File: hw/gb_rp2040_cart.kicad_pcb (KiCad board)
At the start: 4 copper layers, 51.4 x 60.5 mm, 75 parts, among them J1 GameBoy_Cartridge, J2 USB_C_Receptacle_USB2.0, Q1 SI2301CDS-T1-GE3, Q2 N-Channel, SW1 SW_DPST, SW2 SW_Push, U1 SN74LVC8T245PW, U10 MB85RC256VPNF-G-JNERE1, U11 DS3231M, U2 SN74LVC8T245PW, U3 TXU0104, U4 SN74LVC8T245PW, U5 W25Q128JVSIQ, U6 RP2040, U7 XC6206P332MR, U9 PCA9536D, Y1 Crystal_GND24

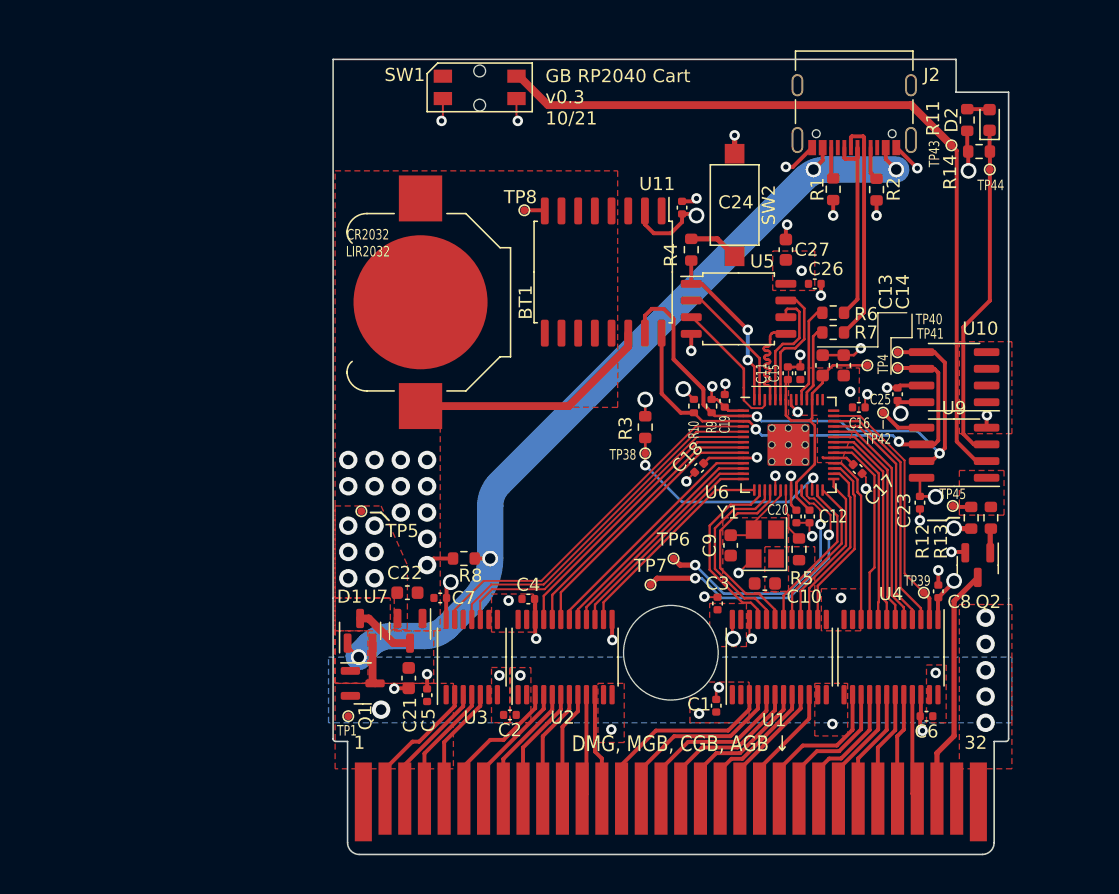
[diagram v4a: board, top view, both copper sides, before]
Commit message: hw: use CR2032 footprint & larger testpoints
Signed-off-by: Mahyar Koshkouei <mk@deltabeard.com>
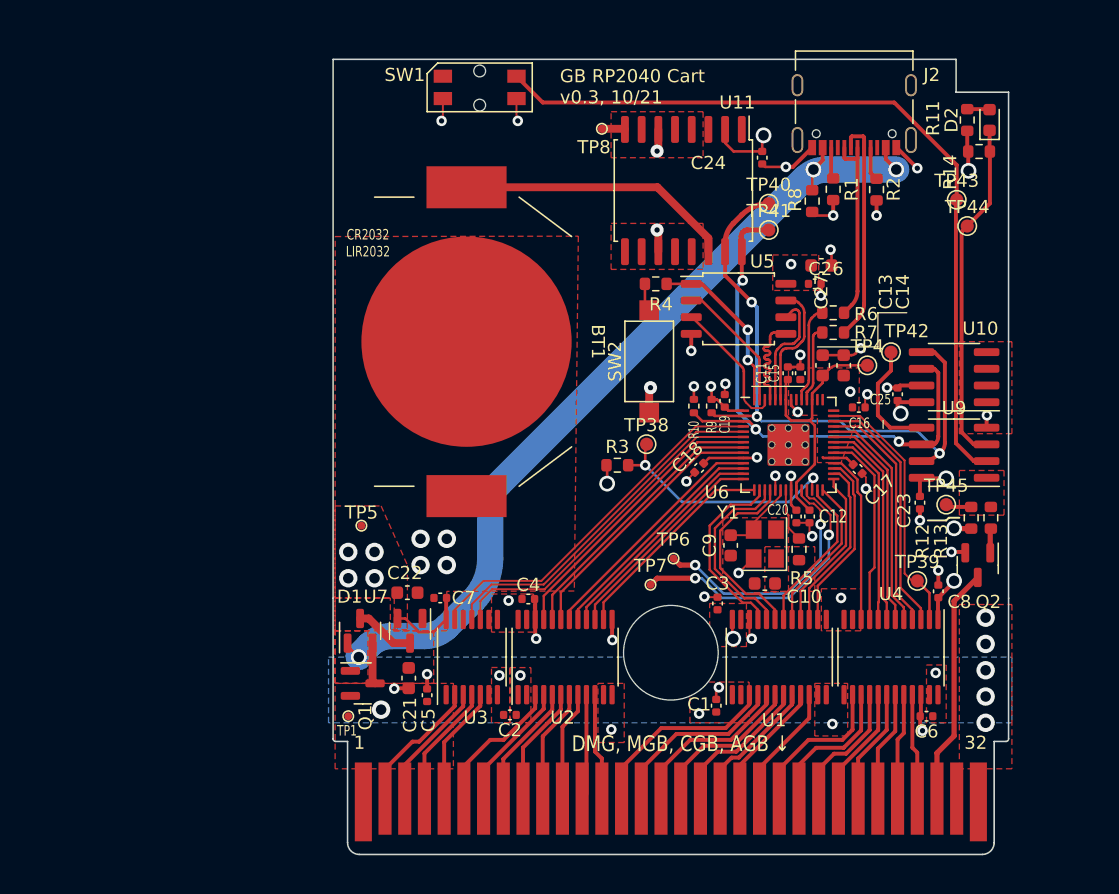
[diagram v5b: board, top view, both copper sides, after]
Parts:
- BT1: footprint Battery:BatteryHolder_Keystone_3000_1x12mm -> Project_Specific:MY-2032-11
- TP38, TP39, TP40, TP41, TP42, TP43, TP44, TP45: footprint Project_Specific:TestPoint_Pad_D0.5mm -> TestPoint:TestPoint_Pad_D1.0mm
- moved R8 38.0 mm to (94.8, 48.3), turned to -90 degrees
- moved TP40 15.0 mm to (91.5, 48.5)
- moved TP41 14.4 mm to (91.5, 50.5)
- moved SW2 13.6 mm to (82.4, 60.5), turned to 90 degrees
- moved U11 8.70 mm to (85.0, 47.5)
- moved TP8 8.56 mm to (78.8, 42.8)
- moved C24 7.19 mm to (91.0, 45.0), turned to -90 degrees
- moved TP42 4.64 mm to (100.8, 59.8)
- moved TP44 4.63 mm to (106.6, 50.2)
- moved BT1 4.61 mm to (68.5, 59.0)
- moved TP43 4.16 mm to (105.8, 48.2)
- moved R4 3.75 mm to (82.9, 54.6), turned to 0 degrees
- moved R3 3.60 mm to (80.0, 68.4), turned to 180 degrees
- moved C27 2.95 mm to (95.5, 53.2), turned to 0 degrees
- moved TP5 1.10 mm to (60.5, 73.0)
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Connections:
- SW1 pad 1: /Peripherals/SWITCH -> (no net)
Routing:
- net /Peripherals/STAT_LED: track 47.3 -> 26.1 mm
- net /Peripherals/SWITCH: track 75.8 -> 60.4 mm
- net I^{2}C_{SCL}: track 35.8 -> 44.0 mm, vias 2 -> 3
- net I^{2}C_{SDA}: track 53.8 -> 47.7 mm, vias 2 -> 3
- net Net-(TP42-Pad1): track 3.40 -> 8.93 mm
- net GND: track 54.0 -> 58.0 mm, vias 54 -> 47
- net Net-(R7-Pad1): track 9.56 -> 5.85 mm
- net +3V3: track 42.3 -> 45.2 mm, vias 23 -> 20
- net /A8: track 15.2 -> 12.5 mm
- net /A14: track 9.82 -> 7.28 mm
- net /A10: track 13.3 -> 10.8 mm
- net /A11: track 12.5 -> 9.95 mm
- net /A12: track 11.6 -> 9.10 mm
- net /A9: track 14.1 -> 11.7 mm
- net /A13: track 10.7 -> 8.25 mm
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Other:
- board text added: "GB RP2040 Cart v0.3, 10/21"
- board text removed: "GB RP2040 Cart v0.3 10/21"
- board text removed: "Order #"

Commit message: More attempts
Signed-off-by: Mahyar Koshkouei <mk@deltabeard.com>
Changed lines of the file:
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@@
   (gr_line (start 100.2 65.6) (end 100.2 65) (layer "F.SilkS") (width 0.1))
   (gr_line (start 105.2 72.4) (end 106 72.4) (layer "F.SilkS") (width 0.15))
+  (gr_line (start 103.6 40.4) (end 109 40.4) (layer "F.SilkS") (width 0.1))
   (gr_line (start 90.2 62.4) (end 94.2 62.4) (layer "F.SilkS") (width 0.1))
   (gr_line (start 99.8 59.4) (end 95.2 59.4) (layer "F.SilkS") (width 0.1))
@@
   (gr_line (start 115 41) (end 53 41) (layer "Eco1.User") (width 0.1))
   (gr_line (start 115 34) (end 53 34) (layer "Eco1.User") (width 0.1))
-  (gr_line (start 103.6 40.4) (end 109 40.4) (layer "Eco2.User") (width 0.1))
   (gr_text "Flash cart compatible with DMG, MGB, CGB, AGB. Unlicensed product.\nUses RP2040 with 16MiB NOR, 32KiB FRAM, RTC, USB-C.\nDesign: United Kingdom, Assembly: P.R. China\nCopyright © 2021 Mahyar Koshkouei; Not for resale." (at 107 94) (layer "B.SilkS")
     (effects (font (size 1 0.85) (thickness 0.14)) (justify left mirror))
@@
   (segment (start 93.925 85.8625) (end 93.925 86.599999) (width 0.3) (layer "F.Cu") (net 27))
   (segment (start 93.925 86.599999) (end 89.297851 91.227148) (width 0.3) (layer "F.Cu") (net 27))
-  (segment (start 94.575 85.8625) (end 94.575 87.642168) (width 0.3) (layer "F.Cu") (net 28))
-  (segment (start 94.575 87.642168) (end 90.797851 91.419317) (width 0.3) (layer "F.Cu") (net 28))
+  (segment (start 94.575 85.8625) (end 94.575 86.895362) (width 0.3) (layer "F.Cu") (net 28))
+  (segment (start 94.575 86.895362) (end 90.797851 90.672511) (width 0.3) (layer "F.Cu") (net 28))
+  (segment (start 90.797851 90.672511) (end 90.797851 91.419317) (width 0.3) (layer "F.Cu") (net 28))
   (segment (start 97.875 88.525) (end 97.1 89.3) (width 0.3) (layer "F.Cu") (net 29))
   (segment (start 97.875 85.8625) (end 97.875 88.525) (width 0.3) (layer "F.Cu") (net 29))

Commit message: hw: begin layout
Signed-off-by: Mahyar Koshkouei <mk@deltabeard.com>
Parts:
- removed C27: 1u, Capacitor_SMD:C_0603_1608Metric
- removed R6: 27.4R, Resistor_SMD:R_0603_1608Metric
- removed SW1: SW_DPST, Project_Specific:K2-1114SA-A4SW-06
- removed TP38, TP39, TP40, TP41, TP42, TP43, TP44, TP45: TestPoint_Small, TestPoint:TestPoint_Pad_D1.0mm
- removed TP4, TP5: TestPoint, TestPoint:TestPoint_Pad_D1.0mm
- removed TP7: SWDIO, TestPoint:TestPoint_Pad_D1.0mm
- removed U10: MB85RC256VPNF-G-JNERE1, Package_SO:SOIC-8_3.9x4.9mm_P1.27mm
- removed U11: DS3231M, Package_SO:SOIC-16W_7.5x10.3mm_P1.27mm
- added SW3: SW_SPST, Project_Specific:TS-1037-A10B3-D2, F.Cu at (61.9, 39.5)
- added TP10: SWCLK, TestPoint:TestPoint_Pad_D1.0mm, F.Cu at (101.8, 45.2)
- added TP11: SWDIO, TestPoint:TestPoint_Pad_D1.0mm, F.Cu at (101.8, 58.1)
- added TP12: GND, TestPoint:TestPoint_Pad_D1.0mm, F.Cu at (101.8, 51.6)
- added TP13: TestPoint_Small, TestPoint:TestPoint_Pad_D1.0mm, F.Cu at (101.8, 53.8)
- added TP14: TestPoint_Small, TestPoint:TestPoint_Pad_D1.0mm, F.Cu at (101.8, 56.0)
- added TP15: TestPoint_Small, TestPoint:TestPoint_Pad_D1.0mm, F.Cu at (101.8, 60.3)
- added TP16: TestPoint_Small, TestPoint:TestPoint_Pad_D1.0mm, F.Cu at (101.8, 64.6)
- added TP9: TestPoint, TestPoint:TestPoint_Pad_D1.0mm, F.Cu at (101.8, 62.4)
- added U8: DS1307Z+, Package_SO:SO-8_3.9x4.9mm_P1.27mm, F.Cu at (60.5, 49.8)
- added Y2: 32.768k-12.5pF, Project_Specific:Crystal_DS26_D2.0mm_L6.0mm_Horizontal_1EP_style1, F.Cu at (65.3, 49.5)
- C10: value 30p -> 100n; footprint Capacitor_SMD:C_0603_1608Metric -> Capacitor_SMD:C_0402_1005Metric
- C11, C12: value 100n -> 30p; footprint Capacitor_SMD:C_0402_1005Metric -> Capacitor_SMD:C_0603_1608Metric
- C13, C14, C21: value 1u -> 100n; footprint Capacitor_SMD:C_0603_1608Metric -> Capacitor_SMD:C_0402_1005Metric
- C15, C23, C24: value 100n -> 1u; footprint Capacitor_SMD:C_0402_1005Metric -> Capacitor_SMD:C_0603_1608Metric
- C9: value 30p -> 1u
- R1, R2: value 5k1 -> 25k; footprint Resistor_SMD:R_0603_1608Metric -> Resistor_SMD:R_0402_1005Metric
- R10, R9: value 4k7 -> 27.4R; footprint Resistor_SMD:R_0402_1005Metric -> Resistor_SMD:R_0603_1608Metric
- R11: value 330R -> 100k
- R14: value 100k -> 330R
- R3: value 100k -> 25k; footprint Resistor_SMD:R_0603_1608Metric -> Resistor_SMD:R_0402_1005Metric
- R4, R5: value 1k -> 5k1
- R7: value 27.4R -> 1k
- R8: value 100k -> 1k
- SW2: value SW_Push -> SW_DIP_x04; footprint Button_Switch_SMD:SW_SPST_CK_RS282G05A3 -> Button_Switch_SMD:SW_DIP_SPSTx04_Slide_6.7x11.72mm_W8.61mm_P2.54mm_LowProfile
- TP1: value TestPoint -> TestPoint_Small
- TP6: value SWCLK -> TestPoint
- TP8: value GND -> TestPoint
- U9: value PCA9536D -> MB85RS256B
- moved R11 79.1 mm to (38.2, 82.0)
- moved C23 65.2 mm to (38.2, 79.0)
- moved C6 62.1 mm to (41.5, 85.0)
- moved C8 61.1 mm to (43.3, 76.5)
- moved C24 57.1 mm to (40.8, 72.3), turned to 180 degrees
- moved R1 51.3 mm to (57.2, 80.5)
- moved R2 45.8 mm to (65.4, 77.8), turned to 90 degrees
- moved U9 42.1 mm to (64.2, 59.8), turned to 0 degrees
- moved R8 41.4 mm to (58.4, 68.0), turned to 0 degrees
- moved C11 41.4 mm to (52.6, 70.5), turned to -90 degrees
- moved C25 38.6 mm to (64.2, 52.2), turned to 0 degrees
- moved C13 38.0 mm to (58.8, 70.2), turned to 180 degrees
- moved C12 37.0 mm to (57.6, 72.3), turned to 90 degrees
- moved TP6 36.9 mm to (101.8, 43.0)
- moved Y1 36.3 mm to (55.1, 70.5)
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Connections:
- BT1 pad 1: Net-(BT1-Pad1) -> V_{BAT}
- C1 pad 1: GB_5V -> +3V3
- C10 pad 1: GND -> +3V3
- C10 pad 2: Net-(C10-Pad2) -> GND
- C11 pad 1: +1V1 -> Net-(C11-Pad1)
- C12 pad 1: +1V1 -> GND
- C12 pad 2: GND -> Net-(C12-Pad2)
- C14 pad 1: +3V3 -> +1V1
- C2 pad 1: GB_5V -> +3V3
- C21 pad 1: +5V -> +3V3
- C22 pad 1: +3V3 -> +1V1
- C23 pad 1: +3V3 -> +5V
- C3 pad 2: +3V3 -> GB_5V
- C4 pad 2: +3V3 -> GB_5V
- C5 pad 1: GB_5V -> GND
- C5 pad 2: GND -> +3V3
- C7 pad 1: GND -> GB_5V
- C7 pad 2: +3V3 -> GND
- C9 pad 1: Net-(C9-Pad1) -> +3V3
- D2 pad 1: /Peripherals/STAT_LED -> Net-(D2-Pad1)
- D2 pad 2: Net-(D2-Pad2) -> STAT_LED
- R1 pad 1: GND -> ADDR1_OE
- R1 pad 2: Net-(J2-PadB5) -> +3V3
- R10 pad 1: I^{2}C_{SCL} -> Net-(R10-Pad1)
- R10 pad 2: +3V3 -> USB_DN
- R11 pad 1: +3V3 -> VBUS
- R11 pad 2: Net-(D2-Pad2) -> GND
- R12 pad 1: /Peripherals/GB_RESET -> GB_RESET
- R13 pad 1: /Peripherals/GB_RESET -> GB_RESET
- R14 pad 1: /Peripherals/STAT_LED -> Net-(D2-Pad1)
- R14 pad 2: +3V3 -> GND
- R2 pad 1: Net-(J2-PadA5) -> ADDR2_OE
- R2 pad 2: GND -> +3V3
- R3 pad 1: /RP2040/RUN -> DATA_OE
- R4 pad 1: /RP2040/USB_BOOT -> GND
- R4 pad 2: /RP2040/QSPI_SS -> Net-(J2-PadB5)
- R5 pad 1: Net-(C10-Pad2) -> Net-(J2-PadA5)
- R5 pad 2: Net-(R5-Pad2) -> GND
- R7 pad 1: Net-(R7-Pad1) -> /RP2040/USB_BOOT
- R7 pad 2: USB_DN -> /RP2040/QSPI_SS
- R8 pad 1: VBUS -> Net-(C12-Pad2)
- R8 pad 2: GND -> Net-(R8-Pad2)
- R9 pad 1: I^{2}C_{SDA} -> Net-(R9-Pad1)
- R9 pad 2: +3V3 -> USB_DP
- SW2 pad 1: GND -> Net-(SW2-Pad1)
- SW2 pad 2: /RP2040/USB_BOOT -> Net-(SW2-Pad2)
- TP1 pad 1: GB_5V -> /A15
- TP6 pad 1: /RP2040/SWCLK -> GB_5V
- TP8 pad 1: GND -> +1V1
- U1 pad 1: GB_5V -> +3V3
- U1 pad 10: /A15 -> 3V3_M0
- U1 pad 14: 3V3_A15 -> /A8
- U1 pad 15: 3V3_A14 -> /A9
- U1 pad 16: 3V3_A13 -> /A10
- U1 pad 17: 3V3_A12 -> /A11
- U1 pad 18: 3V3_A11 -> /A12
- U1 pad 19: 3V3_A10 -> /A13
- U1 pad 2: GB_5V -> GND
- U1 pad 20: 3V3_A9 -> /A14
- U1 pad 21: 3V3_A8 -> /A15
- U1 pad 22: GND -> ADDR2_OE
- U1 pad 23: +3V3 -> GB_5V
- U1 pad 24: +3V3 -> GB_5V
- U1 pad 3: /A8 -> 3V3_M7
- U1 pad 4: /A9 -> 3V3_M6
- U1 pad 5: /A10 -> 3V3_M5
- U1 pad 6: /A11 -> 3V3_M4
- U1 pad 7: /A12 -> 3V3_M3
- U1 pad 8: /A13 -> 3V3_M2
- U1 pad 9: /A14 -> 3V3_M1
- U2 pad 1: GB_5V -> +3V3
- U2 pad 10: /A7 -> 3V3_M0
- U2 pad 14: 3V3_A7 -> /A0
- U2 pad 15: 3V3_A6 -> /A1
- U2 pad 16: 3V3_A5 -> /A2
- U2 pad 17: 3V3_A4 -> /A3
- U2 pad 18: 3V3_A3 -> /A4
- U2 pad 19: 3V3_A2 -> /A5
- U2 pad 2: GB_5V -> GND
- U2 pad 20: 3V3_A1 -> /A6
- U2 pad 21: 3V3_A0 -> /A7
- U2 pad 22: GND -> ADDR1_OE
- U2 pad 23: +3V3 -> GB_5V
- U2 pad 24: +3V3 -> GB_5V
- U2 pad 3: /A0 -> 3V3_M7
- U2 pad 4: /A1 -> 3V3_M6
- U2 pad 5: /A2 -> 3V3_M5
- U2 pad 6: /A3 -> 3V3_M4
- U2 pad 7: /A4 -> 3V3_M3
- U2 pad 8: /A5 -> 3V3_M2
- U2 pad 9: /A6 -> 3V3_M1
- U4 pad 10: 3V3_D0 -> 3V3_M0
- U4 pad 22: GND -> DATA_OE
- U4 pad 3: 3V3_D7 -> 3V3_M7
- U4 pad 4: 3V3_D6 -> 3V3_M6
- U4 pad 5: 3V3_D5 -> 3V3_M5
- U4 pad 6: 3V3_D4 -> 3V3_M4
- U4 pad 7: 3V3_D3 -> 3V3_M3
- U4 pad 8: 3V3_D2 -> 3V3_M2
- U4 pad 9: 3V3_D1 -> 3V3_M1
- U6 pad 11: 3V3_A3 -> unconnected-(U6-Pad11)
- U6 pad 12: 3V3_A4 -> SWITCH
- U6 pad 13: 3V3_A5 -> I2C_{SDA}
- U6 pad 14: 3V3_A6 -> I2C_{SCLK}
- U6 pad 15: 3V3_A7 -> PHI_3V3
- U6 pad 16: 3V3_A8 -> ~{WR}_3V3
- U6 pad 17: 3V3_A9 -> ~{RD}_3V3
- U6 pad 18: 3V3_A10 -> ~{CS}_3V3
- U6 pad 2: I^{2}C_{SDA} -> Net-(SW2-Pad1)
- U6 pad 20: Net-(C9-Pad1) -> Net-(C11-Pad1)
- U6 pad 21: Net-(R5-Pad2) -> Net-(R8-Pad2)
- U6 pad 26: /RP2040/RUN -> unconnected-(U6-Pad26)
- U6 pad 27: 3V3_A11 -> ADDR1_OE
- U6 pad 28: 3V3_A12 -> ADDR2_OE
- U6 pad 29: 3V3_A13 -> DATA_OE
- U6 pad 3: I^{2}C_{SCL} -> Net-(SW2-Pad2)
- U6 pad 30: 3V3_A14 -> DATA_DIR
- U6 pad 31: 3V3_A15 -> 3V3_M0
- U6 pad 32: 3V3_D0 -> 3V3_M1
- U6 pad 34: 3V3_D1 -> 3V3_M2
- U6 pad 35: 3V3_D2 -> 3V3_M3
- U6 pad 36: 3V3_D3 -> 3V3_M4
- U6 pad 37: 3V3_D4 -> 3V3_M5
- U6 pad 38: 3V3_D5 -> 3V3_M6
- U6 pad 39: 3V3_D6 -> 3V3_M7
- U6 pad 4: PHI_3V3 -> Net-(SW2-Pad3)
- U6 pad 40: 3V3_D7 -> GB_RESET
- U6 pad 41: DATA_DIR -> STAT_LED
- U6 pad 46: Net-(R7-Pad1) -> Net-(R10-Pad1)
- U6 pad 47: Net-(R6-Pad1) -> Net-(R9-Pad1)
- U6 pad 5: ~{RD}_3V3 -> unconnected-(U6-Pad5)
- U6 pad 6: ~{CS}_3V3 -> SPI0_{MISO}
- U6 pad 7: 3V3_A0 -> SPI0_{CSn}
- U6 pad 8: 3V3_A1 -> SPI0_{SCK}
- U6 pad 9: 3V3_A2 -> SPI0_{MOSI}
- U9 pad 1: /Peripherals/GB_RESET -> SPI0_{CSn}
- U9 pad 2: /Peripherals/SWITCH -> SPI0_{MISO}
- U9 pad 3: /Peripherals/STAT_LED -> +3V3
- U9 pad 5: Net-(TP42-Pad1) -> SPI0_{MOSI}
- U9 pad 6: I^{2}C_{SCL} -> SPI0_{SCK}
- U9 pad 7: I^{2}C_{SDA} -> +3V3
- Y1 pad 1: Net-(C10-Pad2) -> Net-(C12-Pad2)
- Y1 pad 3: Net-(C9-Pad1) -> Net-(C11-Pad1)
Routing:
- net VBUS: track 66.5 -> 6.05 mm, vias 3 -> 0
- net /Peripherals/SWITCH: track 60.4 -> 0.00 mm
- net GND: track 58.0 -> 6.03 mm, vias 47 -> 9
- net I^{2}C_{SDA}: track 47.7 -> 0.00 mm, vias 3 -> 0
- net 3V3_M2: track 0.00 -> 46.2 mm, vias 0 -> 3
- net 3V3_M1: track 0.00 -> 45.4 mm, vias 0 -> 3
- net I^{2}C_{SCL}: track 44.0 -> 0.00 mm, vias 3 -> 0
- net 3V3_M3: track 0.00 -> 43.8 mm, vias 0 -> 3
- net 3V3_M0: track 0.00 -> 43.4 mm, vias 0 -> 2
- net 3V3_M4: track 0.00 -> 43.0 mm, vias 0 -> 3
- net 3V3_M6: track 0.00 -> 41.1 mm, vias 0 -> 3
- net 3V3_M5: track 0.00 -> 39.6 mm, vias 0 -> 3
- net 3V3_M7: track 0.00 -> 37.7 mm, vias 0 -> 3
- net DATA_OE: track 0.00 -> 35.9 mm, vias 0 -> 2
- net +3V3: track 45.2 -> 12.2 mm, vias 20 -> 0
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- removed copper zone on F.Cu, net +3V3
- removed copper zone on In2.Cu, net +3V3
- removed copper zone on F.Cu, net +5V
- removed copper zone on F.Cu, net /Peripherals/GB_RESET
- removed copper zone on B.Cu, net GB_5V
- removed copper zone on F.Cu, net GB_5V
- removed copper zone on In1.Cu, net GND
- removed copper zone on F.Cu, net Net-(C10-Pad2)
- removed copper zone on F.Cu, net VBUS
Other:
- board size 51.4 x 60.5 mm -> 51.4 x 60.6 mm
- copper layers 4 -> 2
- board text removed: "CR2032 LIR2032"
- board text removed: "DMG, MGB, CGB, AGB ↓"
- board text removed: "Flash cart compatible with DMG, MGB, CGB, AGB. Unlicensed product. Uses RP2040 with 16MiB NOR, 32KiB FRAM, RTC, USB-C. Design: United Kingdom, Assembly: P.R. China Copyright © 2021 Mahyar Koshkouei; Not for resale."
- board text removed: "GB RP2040 Cart v0.3, 10/21"
- board text removed: "JLCJLCJLCJLC"
- board text removed: "git.io/JEM5x"

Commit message: hw: WIP
Signed-off-by: Mahyar Koshkouei <mk@deltabeard.com>
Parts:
- removed SW3: SW_SPST, Project_Specific:TS-1037-A10B3-D2
- removed TP12: GND, TestPoint:TestPoint_Pad_D1.0mm
- removed TP13, TP14, TP15, TP16: TestPoint_Small, TestPoint:TestPoint_Pad_D1.0mm
- added C27: 100n, Capacitor_SMD:C_0402_1005Metric, F.Cu at (43.8, 72.7)
- added D3: SM4007PL, Diode_SMD:D_SOD-123F, F.Cu at (41.4, 70.5)
- added M1: Motor_DC, Connector_PinHeader_1.27mm:PinHeader_1x02_P1.27mm_Vertical, F.Cu at (38.6, 71.3)
- added Q3: N-Channel, Package_TO_SOT_SMD:SOT-23, F.Cu at (44.5, 70.5)
- added R6: 1k, Resistor_SMD:R_0603_1608Metric, F.Cu at (73.8, 52.2)
- added SW1: SW_DIP_x04, Button_Switch_SMD:SW_DIP_SPSTx04_Slide_6.7x11.72mm_W8.61mm_P2.54mm_LowProfile, F.Cu at (81.5, 53.0)
- added TP2: TestPoint, TestPoint:TestPoint_Pad_D1.0mm, F.Cu at (114.5, 57.4)
- added TP3: TestPoint, TestPoint:TestPoint_THTPad_D1.0mm_Drill0.5mm, F.Cu at (99.7, 61.5)
- added TP4: TestPoint, TestPoint:TestPoint_THTPad_D1.0mm_Drill0.5mm, F.Cu at (105.8, 57.4)
- added TP5: TestPoint, TestPoint:TestPoint_THTPad_D1.0mm_Drill0.5mm, F.Cu at (101.8, 59.5)
- added TP7: TestPoint, TestPoint:TestPoint_THTPad_D1.0mm_Drill0.5mm, F.Cu at (99.7, 59.5)
- C11, C12, C15, C22, C23, C24, C9: footprint Capacitor_SMD:C_0603_1608Metric -> Capacitor_SMD:C_0402_1005Metric
- R10: value 27.4R -> 100k
- R12: value 100k -> 330R
- R4, R5: footprint Resistor_SMD:R_0603_1608Metric -> Resistor_SMD:R_0402_1005Metric
- R8: value 1k -> 27.4R
- SW2: value SW_DIP_x04 -> SW_SPST; footprint Button_Switch_SMD:SW_DIP_SPSTx04_Slide_6.7x11.72mm_W8.61mm_P2.54mm_LowProfile -> Button_Switch_SMD:SW_SPST_TL3342
- TP1: value TestPoint_Small -> TestPoint
- TP10: value SWCLK -> TestPoint
- TP11: value SWDIO -> TestPoint
- TP6: footprint TestPoint:TestPoint_Pad_D1.0mm -> TestPoint:TestPoint_THTPad_D1.0mm_Drill0.5mm
- moved R11 47.6 mm to (85.8, 79.5), turned to 0 degrees
- moved R14 46.8 mm to (48.0, 69.5)
- moved R13 40.5 mm to (85.0, 40.5), turned to 180 degrees
- moved R10 38.5 mm to (38.3, 85.2)
- moved R8 26.9 mm to (85.3, 68.2)
- moved SW2 23.6 mm to (61.9, 43.0)
- moved R7 19.5 mm to (58.3, 68.0), turned to 0 degrees
- moved TP6 18.5 mm to (101.8, 61.5)
- moved TP10 12.2 mm to (101.8, 57.4)
- moved R9 12.0 mm to (85.3, 69.7)
- moved TP8 9.58 mm to (103.8, 57.4)
- moved U5 5.15 mm to (74.0, 67.0)
- moved TP9 3.63 mm to (103.8, 59.5)
- moved C24 3.34 mm to (43.3, 74.5), turned to -90 degrees
- moved C10 3.25 mm to (80.0, 66.5)
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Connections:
- R10 pad 1: Net-(R10-Pad1) -> VBUS
- R10 pad 2: USB_DN -> GND
- R11 pad 1: VBUS -> GB_RESET
- R11 pad 2: GND -> +3V3
- R12 pad 2: +3V3 -> Net-(Q2-Pad1)
- R13 pad 1: GB_RESET -> Net-(D2-Pad1)
- R13 pad 2: Net-(Q2-Pad1) -> GND
- R14 pad 1: Net-(D2-Pad1) -> MOTOR
- R14 pad 2: GND -> Net-(Q3-Pad1)
- R7 pad 1: /RP2040/USB_BOOT -> Net-(C12-Pad2)
- R7 pad 2: /RP2040/QSPI_SS -> Net-(R7-Pad2)
- R8 pad 1: Net-(C12-Pad2) -> Net-(R8-Pad1)
- R8 pad 2: Net-(R8-Pad2) -> USB_DP
- R9 pad 2: USB_DP -> USB_DN
- SW2 pad 1: Net-(SW2-Pad1) -> SWITCH
- SW2 pad 2: Net-(SW2-Pad2) -> GND
- TP10 pad 1: /RP2040/SWCLK -> DATA_OE
- TP11 pad 1: /RP2040/SWDIO -> DATA_DIR
- TP6 pad 1: GB_5V -> /RP2040/SWDIO
- TP8 pad 1: +1V1 -> ADDR1_OE
- TP9 pad 1: +3V3 -> ADDR2_OE
- U6 pad 11: unconnected-(U6-Pad11) -> I2C_{SDA}
- U6 pad 12: SWITCH -> I2C_{SCLK}
- U6 pad 13: I2C_{SDA} -> SWITCH
- U6 pad 14: I2C_{SCLK} -> MOTOR
- U6 pad 2: Net-(SW2-Pad1) -> Net-(SW1-Pad1)
- U6 pad 21: Net-(R8-Pad2) -> Net-(R7-Pad2)
- U6 pad 3: Net-(SW2-Pad2) -> Net-(SW1-Pad2)
- U6 pad 4: Net-(SW2-Pad3) -> Net-(SW1-Pad3)
- U6 pad 46: Net-(R10-Pad1) -> Net-(R9-Pad1)
- U6 pad 47: Net-(R9-Pad1) -> Net-(R8-Pad1)
- U6 pad 5: unconnected-(U6-Pad5) -> SPI0_{MOSI}
- U6 pad 9: SPI0_{MOSI} -> unconnected-(U6-Pad9)
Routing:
- net VBUS: track 6.05 -> 91.7 mm, vias 0 -> 2
- net USB_DN: track 35.3 -> 2.47 mm
- net USB_DP: track 34.4 -> 2.47 mm
- net MOTOR: track 0.00 -> 15.0 mm
- net I2C_{SDA}: track 13.4 -> 0.00 mm
- net +5V: track 3.02 -> 15.2 mm
- net GND: track 6.03 -> 17.8 mm, vias 9 -> 18
- net SPI0_{CSn}: track 0.00 -> 10.2 mm
- net Net-(C27-Pad1): track 0.00 -> 8.45 mm
- net +3V3: track 12.2 -> 19.9 mm
- net SPI0_{MISO}: track 0.00 -> 7.02 mm
- net SPI0_{SCK}: track 0.00 -> 6.53 mm, vias 0 -> 2
- net Net-(R9-Pad1): track 5.25 -> 0.00 mm
- net Net-(R10-Pad1): track 5.07 -> 0.00 mm
- net SPI0_{MOSI}: track 0.00 -> 3.59 mm
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- added copper zone on B.Cu, net GND
